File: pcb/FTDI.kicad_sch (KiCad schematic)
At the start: 53 parts, among them J4 USB3_B_micro, Q1 Q_NMOS_GSD, U5 ECMF02-4CMX8, U6 ECMF04-4HSWM10, U7 FT600Q-B-x, Y1 30MHz

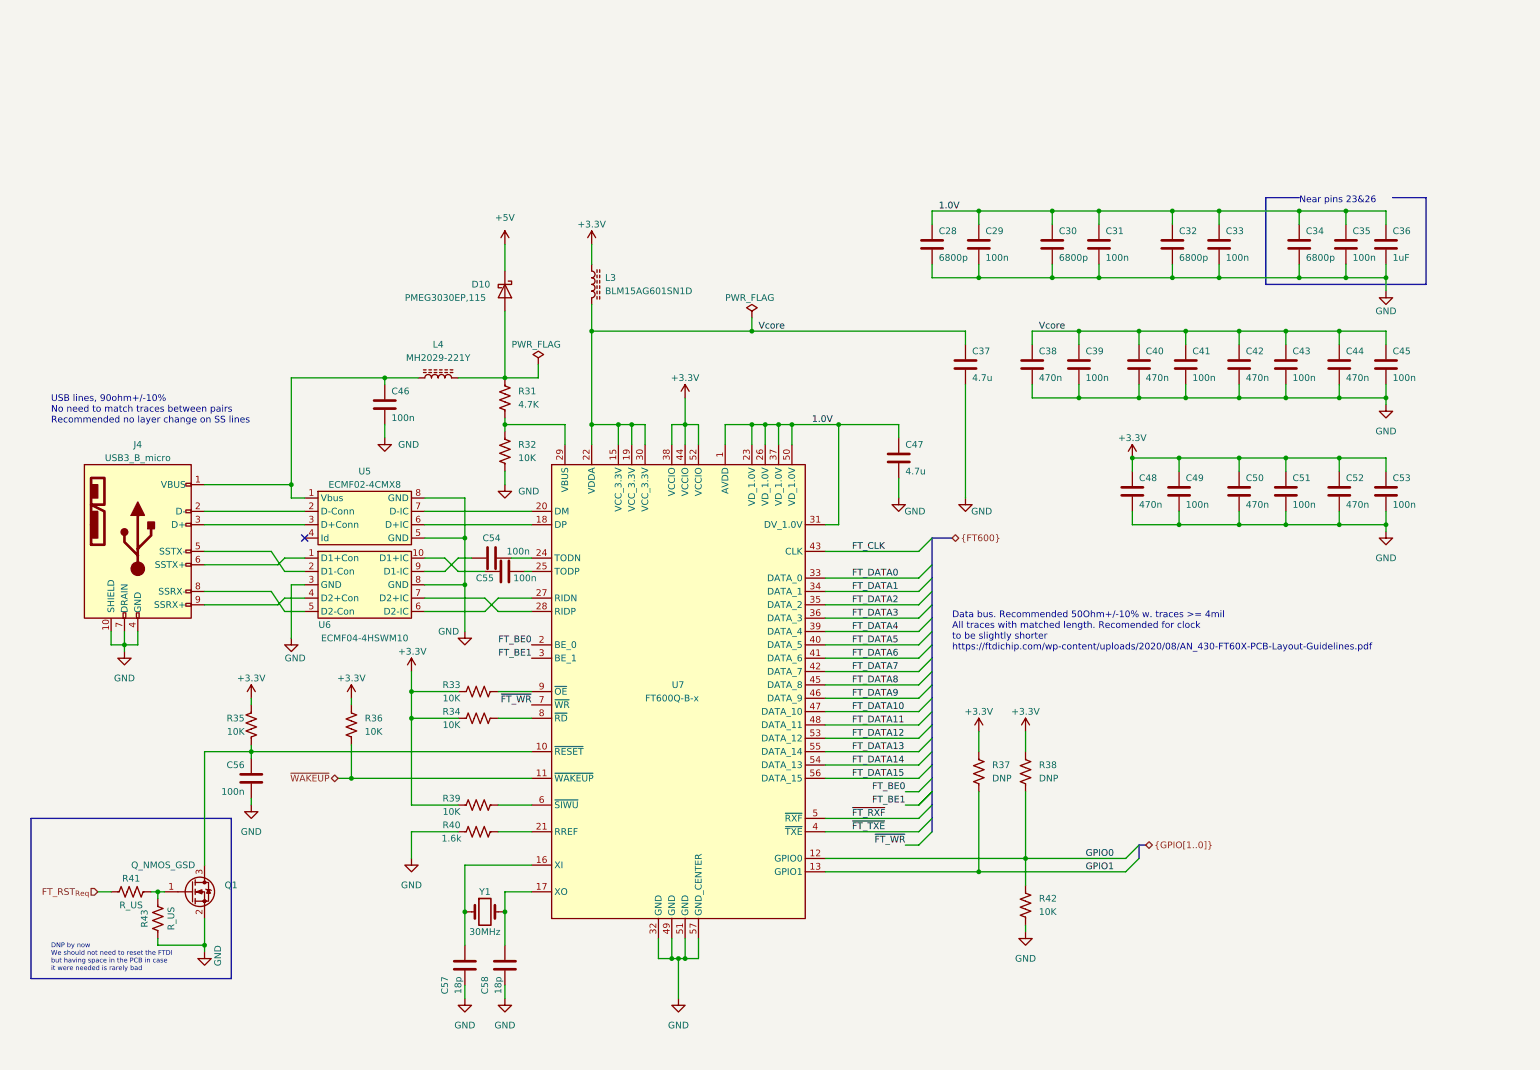
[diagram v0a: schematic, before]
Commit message: Rough PCB component placement
- This will change
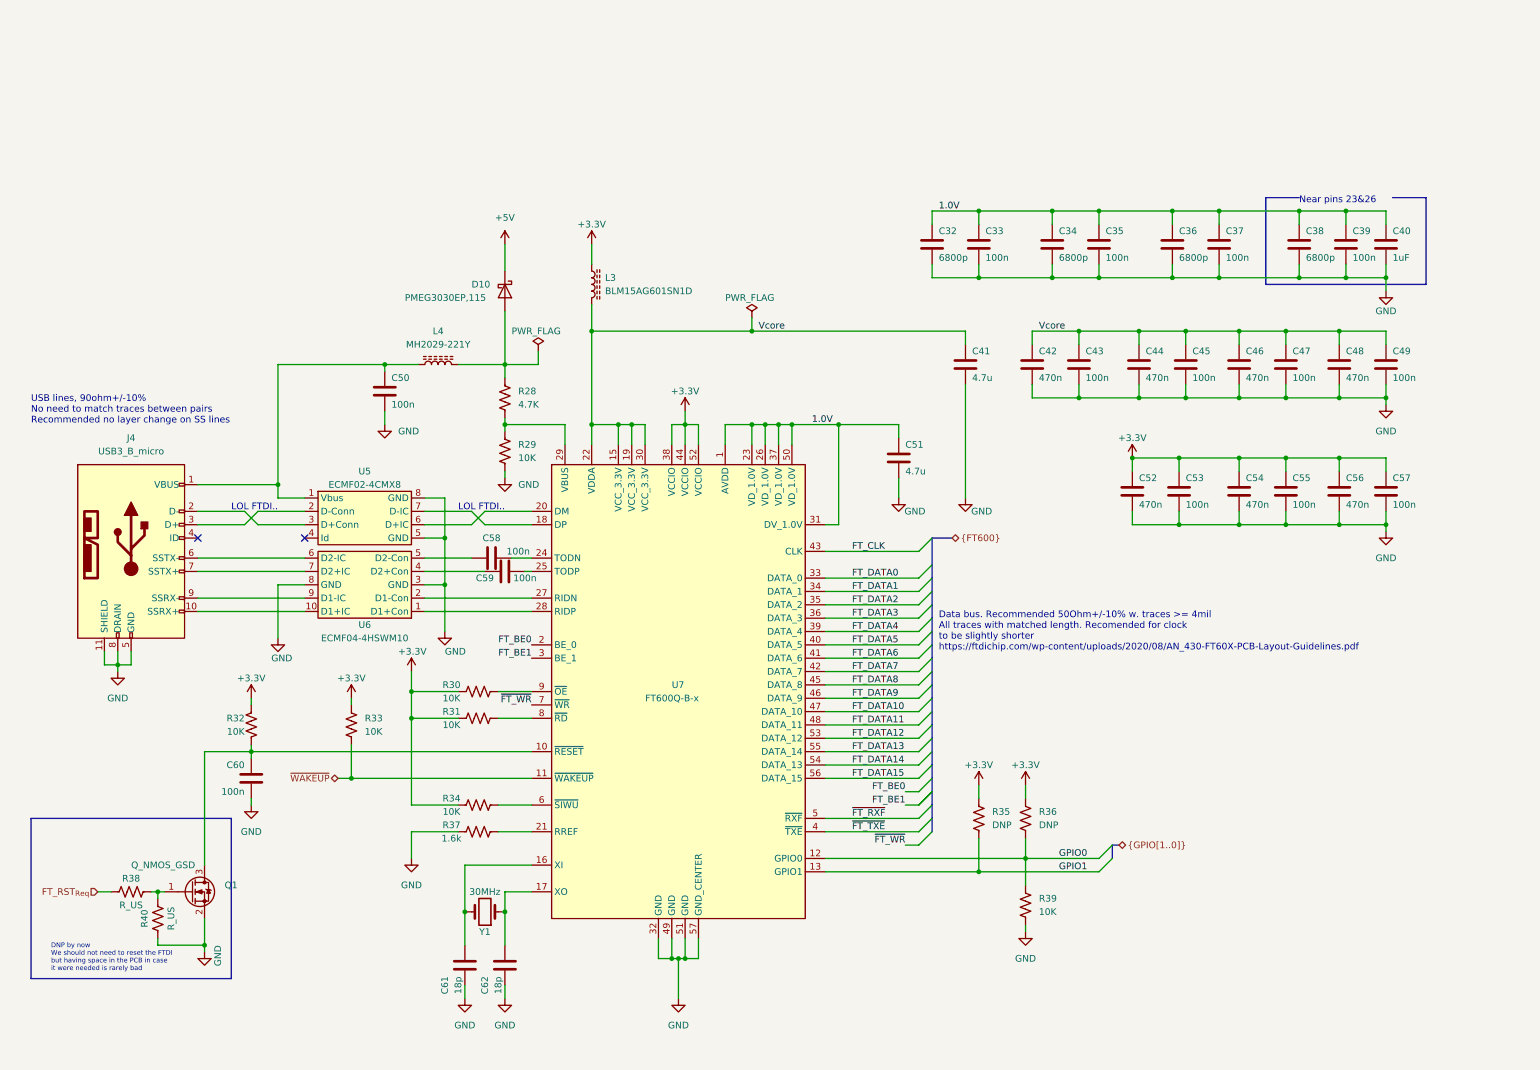
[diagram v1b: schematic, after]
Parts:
- removed J4: USB3_B_micro, Connector_USB:USB_Micro-B_Wuerth_629105150521, symbol ecp5u85-bse-usb:USB3_B_micro
- added J4: USB3_B_micro, jonnew:HIROSE_ZX360D-B-10P, symbol jonnew:USB3_B_micro
- C40: renamed from C36; footprint Capacitor_SMD:C_0805_2012Metric -> Capacitor_SMD:C_0603_1608Metric
- C41: renamed from C37; footprint Capacitor_SMD:C_1210_3225Metric -> Capacitor_SMD:C_0805_2012Metric
- C51: renamed from C47; footprint Capacitor_SMD:C_1210_3225Metric -> Capacitor_SMD:C_0805_2012Metric
- renumbered C28 to C32, C29 to C33, C30 to C34, C31 to C35, C32 to C36, C33 to C37, C34 to C38, C35 to C39, C38 to C42, C39 to C43, C40 to C44, C41 to C45, C42 to C46, C43 to C47, C44 to C48, C45 to C49, C46 to C50, C48 to C52, C49 to C53, C50 to C54, C51 to C55, C52 to C56, C53 to C57, C54 to C58, C55 to C59, C56 to C60, C57 to C61, C58 to C62, R31 to R28, R32 to R29, R33 to R30, R34 to R31, R35 to R32, R36 to R33, R39 to R34, R37 to R35, R38 to R36, R40 to R37, R41 to R38, R42 to R39, R43 to R40
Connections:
- net GND: now also J4.11 (SHIELD), J4.5 (GND), J4.8 (DRAIN)
- net at C50.1, L4.1, U5.1 (Vbus): now also J4.1 (VBUS)
- net at U5.2 (D-Conn): now also J4.3 (D+)
- net at U5.3 (D+Conn): now also J4.2 (D-)
- net at U5.6 (D+IC): now also U7.20 (DM); no longer U7.18 (DP)
- net at U5.7 (D-IC): now also U7.18 (DP); no longer U7.20 (DM)
- net at C61.2, U7.16 (XI): now also Y1.2; no longer Y1.1
- net at C62.2, U7.17 (XO): now also Y1.1; no longer Y1.2
- net at U7.27 (RIDN): now also U6.2 (D1-Con); no longer U6.6 (D2-IC)
- net at U7.28 (RIDP): now also U6.1 (D1+Con); no longer U6.7 (D2+IC)
- net at C59.1: now also U6.4 (D2+Con); no longer U6.10 (D1+IC)
- net at U6.5 (D2-Con): now also C58.1
- net at U6.9 (D1-IC): now also J4.9 (SSRX-); no longer C58.1
- new net: J4.10 (SSRX+), U6.10 (D1+IC)
- new net: J4.6 (SSTX-), U6.6 (D2-IC)
- new net: J4.7 (SSTX+), U6.7 (D2+IC)
- no-connect marks 1 -> 2
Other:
- note added: "LOL FTDI.."
- moved on the sheet: C50, L4, R35, R36, Y1

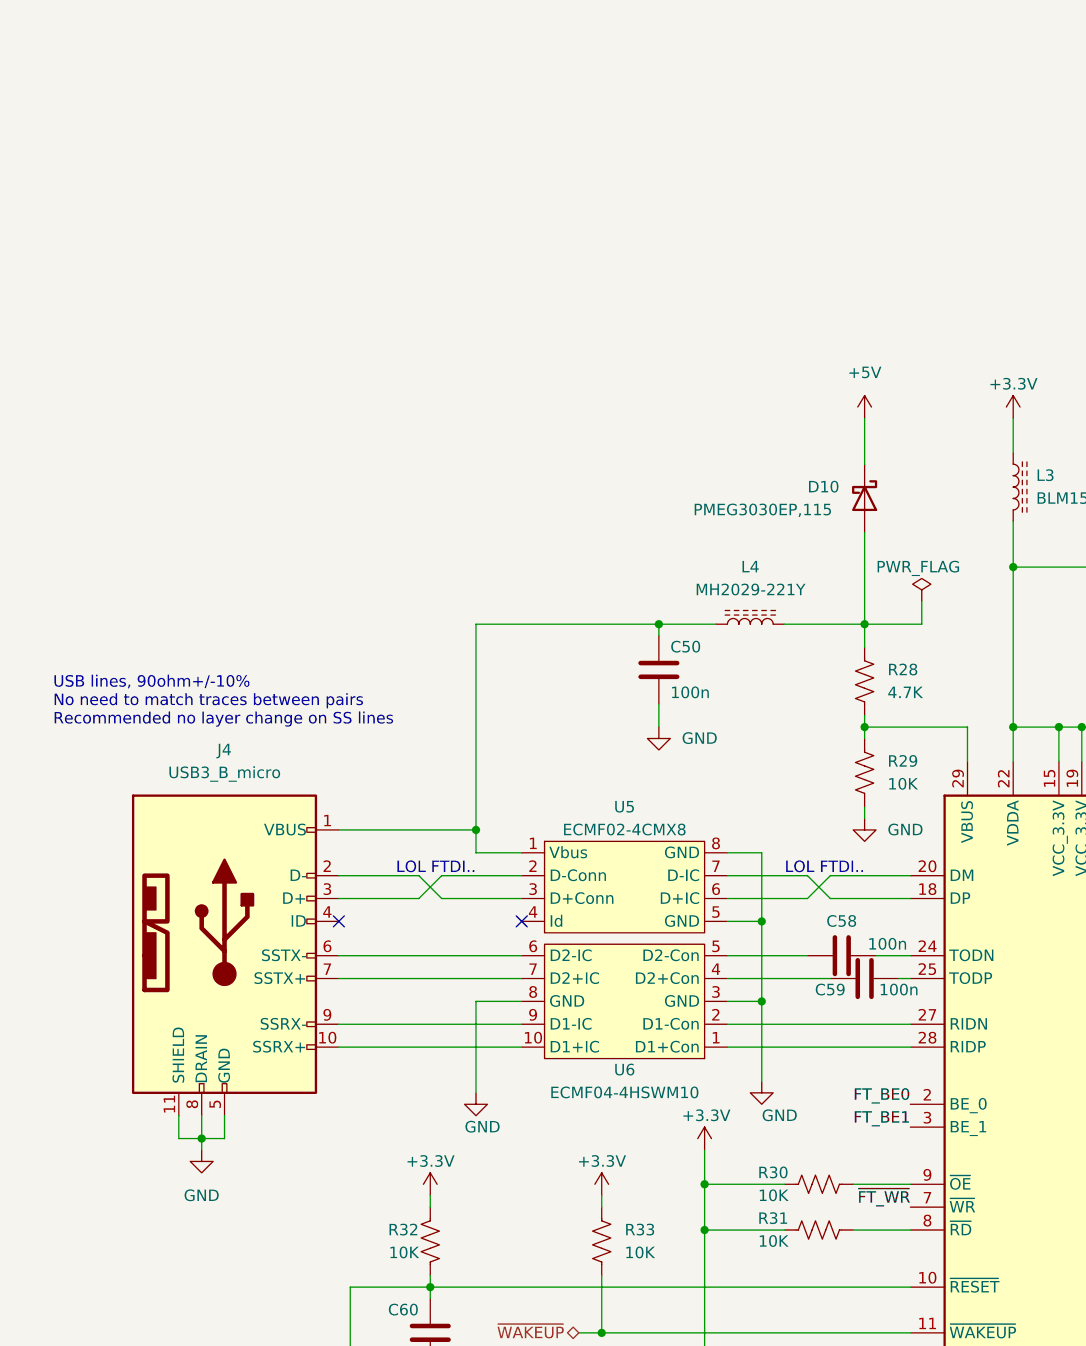
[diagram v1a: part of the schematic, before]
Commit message: Performed rough RAM routing
- Traces 25 mm long, all matched.
- No power routed yet but I want to confirm that FPGA pin remap before
going forward because I can probably make this work.
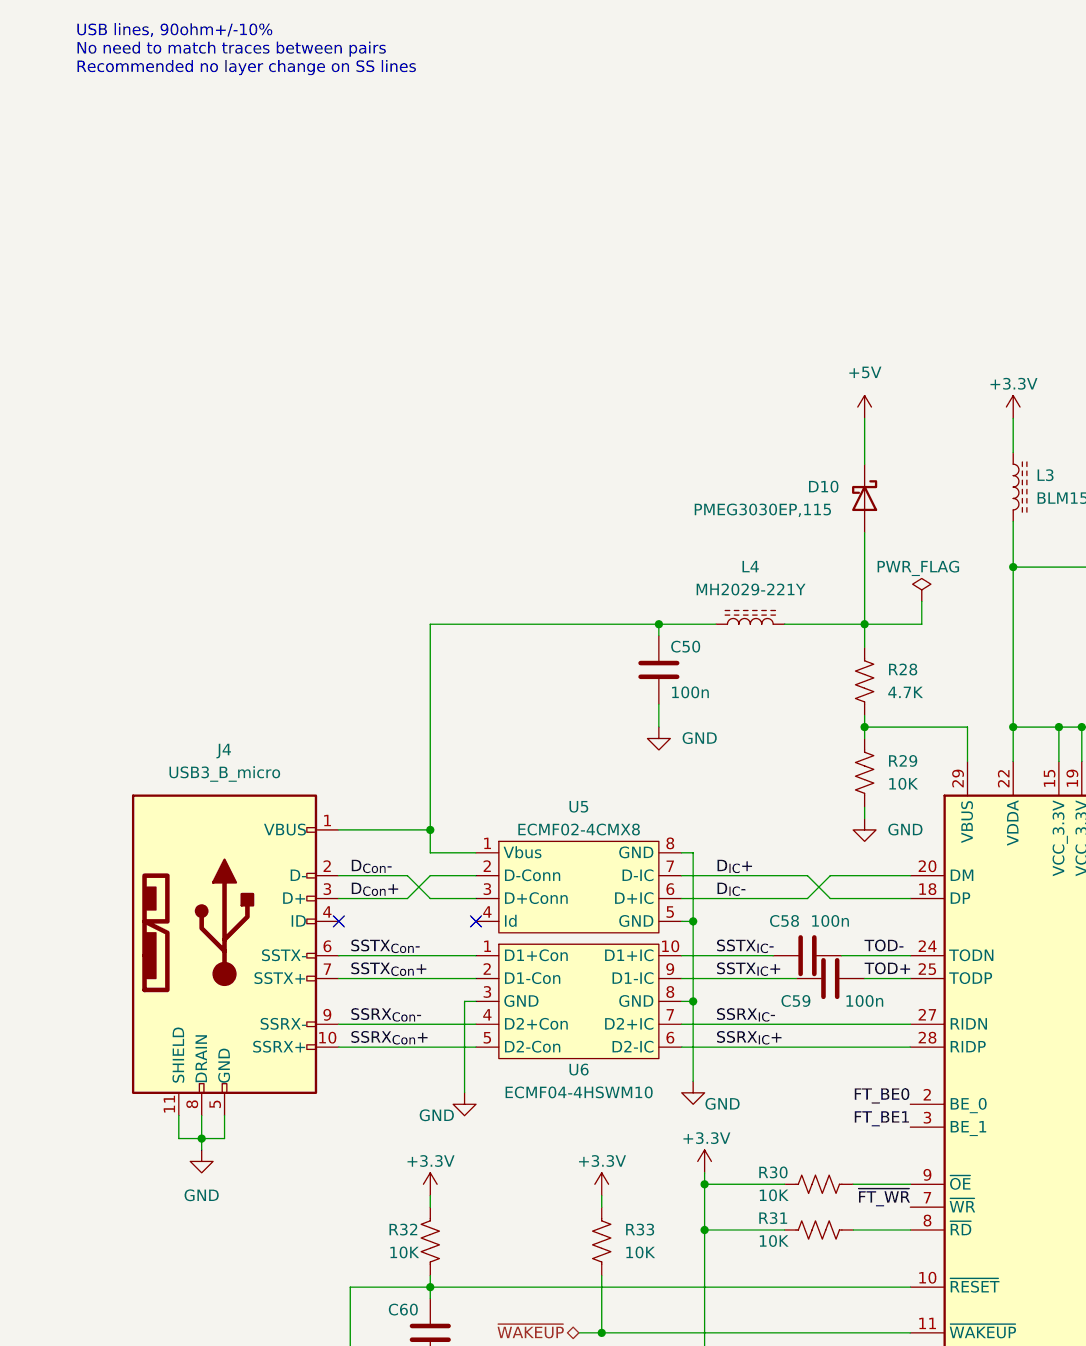
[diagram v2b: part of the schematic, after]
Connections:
- net D_{Con}+: now reaches J4.3 (D+), U5.2 (D-Conn)
- net D_{Con}-: now reaches J4.2 (D-), U5.3 (D+Conn)
- net D_{IC}-: now reaches U5.6 (D+IC), U7.20 (DM)
- net D_{IC}+: now reaches U5.7 (D-IC), U7.18 (DP)
- net TOD-: now reaches C58.2, U7.24 (TODN)
- net TOD+: now reaches C59.2, U7.25 (TODP)
- net SSRX_{IC}-: now reaches U7.27 (RIDN)
- net SSRX_{IC}-: now also U6.7 (D2+IC); no longer U6.2 (D1-Con)
- net SSRX_{IC}+: now reaches U7.28 (RIDP)
- net SSRX_{IC}+: now also U6.6 (D2-IC); no longer U6.1 (D1+Con)
- net SSRX_{Con}-: now reaches U6.4 (D2+Con)
- net SSRX_{Con}-: now also J4.9 (SSRX-); no longer C59.1
- net SSRX_{Con}+: now reaches J4.10 (SSRX+)
- net SSRX_{Con}+: now also U6.5 (D2-Con); no longer U6.10 (D1+IC)
- net SSTX_{IC}-: now reaches C58.1
- net SSTX_{IC}-: now also U6.10 (D1+IC); no longer U6.5 (D2-Con)
- net SSTX_{Con}-: now reaches J4.6 (SSTX-)
- net SSTX_{Con}-: now also U6.1 (D1+Con); no longer U6.6 (D2-IC)
- net SSTX_{Con}+: now reaches J4.7 (SSTX+)
- net SSTX_{Con}+: now also U6.2 (D1-Con); no longer U6.7 (D2+IC)
- net SSTX_{IC}+: now reaches U6.9 (D1-IC)
- net SSTX_{IC}+: now also C59.1; no longer J4.9 (SSRX-)
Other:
- note removed: "LOL FTDI.."
- moved on the sheet: C58, C59, U5, U6

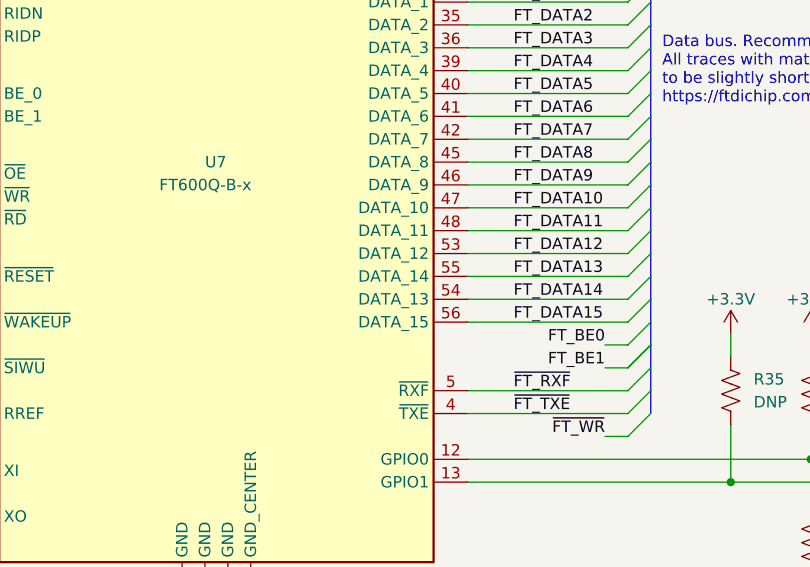
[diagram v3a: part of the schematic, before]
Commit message: FTDI FIFO bus to FPGA routing
- Needs FPGA pin review
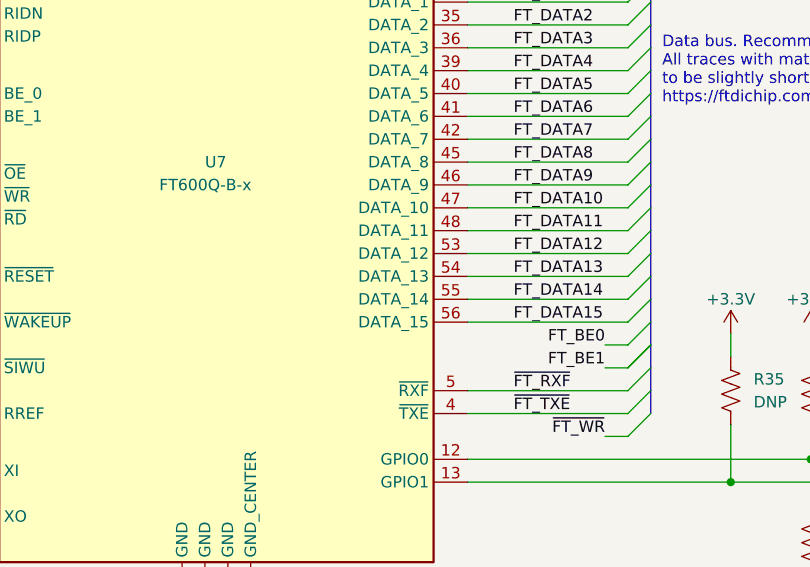
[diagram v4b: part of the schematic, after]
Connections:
- net FT_DATA13: now also U7.54 (DATA_13); no longer U7.55 (DATA_14)
- net FT_DATA14: now also U7.55 (DATA_14); no longer U7.54 (DATA_13)

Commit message: Rev. A before fab comments
- Added gerbers, mount positions, etc.
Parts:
- removed Y1: 30MHz, Crystal:Crystal_SMD_5032-4Pin_5.0x3.2mm, symbol Device:Crystal
- added Y1: ABM8G-30.000MHZ-18-D2Y-T, Crystal:Crystal_SMD_Abracon_ABM8G-4Pin_3.2x2.5mm, symbol Device:Crystal_GND24
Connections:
- net GND: now also Y1.2, Y1.4
- net XI: now reaches C61.2, U7.16 (XI)
- net XI: now also Y1.1
- net XO: now reaches C62.2, U7.17 (XO)
- net XO: now also Y1.3
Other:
- moved on the sheet: C61, C62

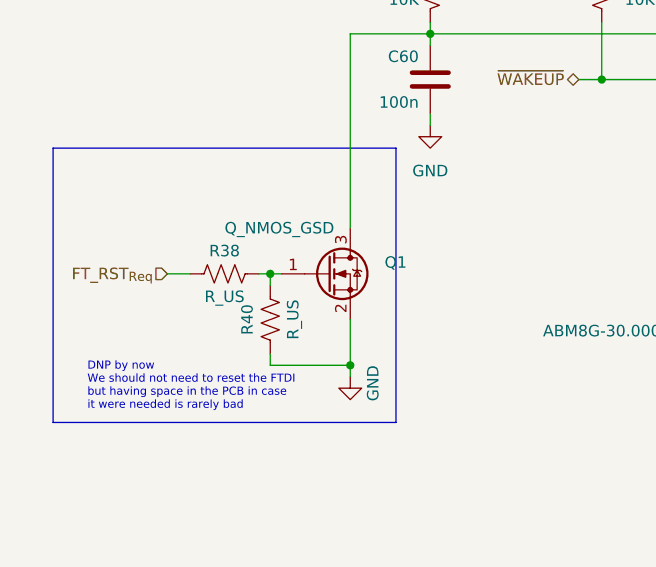
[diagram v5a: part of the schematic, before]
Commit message: Started revision B
- D8 polarity was reversed
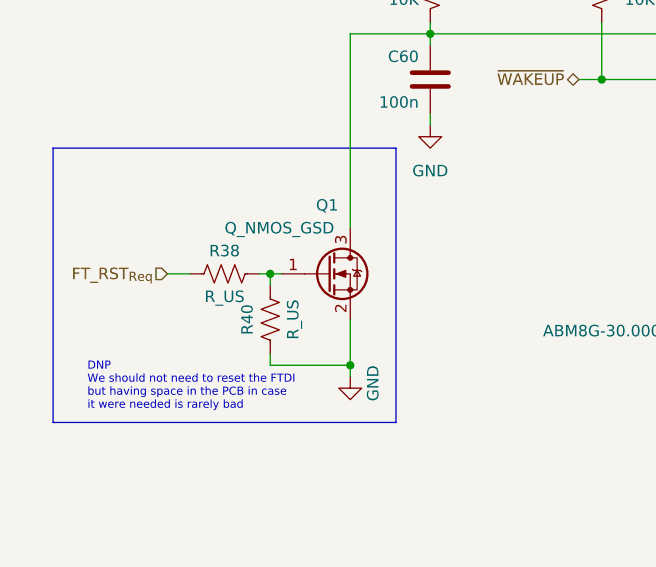
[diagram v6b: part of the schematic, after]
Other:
- note added: "DNP We should not need to reset the FTDI but having space in the PCB in case it were needed is rarely bad"
- note removed: "DNP by now We should not need to reset the FTDI but having space in the PCB in case it were needed is rarely bad"
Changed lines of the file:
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@@
     (title "ECP5U85-BSE-USB Breakout Board")
     (date "2022-02-02")
-    (rev "A")
+    (rev "B")
     (company "OEPS & Open Ephys, Inc.")
     (comment 1 "Jonathan Newman")
@@
     (stroke (width 0) (type default) (color 0 0 0 0))
   )
-  (text "DNP by now\nWe should not need to reset the FTDI\nbut having space in the PCB in case\nit were needed is rarely bad"
+  (text "DNP\nWe should not need to reset the FTDI\nbut having space in the PCB in case\nit were needed is rarely bad"
     (at 20.32 163.83 0)
     (effects (font (size 0.9 0.9)) (justify left bottom))
@@
   (symbol (lib_id "Device:Q_NMOS_GSD") (at 46.99 148.59 0) (unit 1)
     (in_bom yes) (on_board yes)
-    (property "Reference" "Q1" (id 0) (at 53.34 147.3199 0)
-      (effects (font (size 1.27 1.27)) (justify left))
-    )
+    (property "Reference" "Q1" (id 0) (at 45.72 140.97 0)
+      (effects (font (size 1.27 1.27)) (justify left))
+    )
